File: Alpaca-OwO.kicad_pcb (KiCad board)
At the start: 4 copper layers, 100 x 45 mm, 43 parts, among them J1 SWD, J2 PS360 ST1, J3 PS360 ST2, J4 Stick, J5 USB_B, J6 Pwny Pr0t, J7 I2C Quick connect, Q1 CJL3415, SW1 Reset, SW2 I2C Pullup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

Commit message: Coarse placement
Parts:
- moved H2 118.6 mm to (115.0, 51.5)
- moved H4 115.6 mm to (206.0, 89.0)
- moved C14 88.3 mm to (161.8, 73.0), turned to 180 degrees
- moved C7 88.1 mm to (161.8, 71.5)
- moved H1 87.9 mm to (115.0, 89.5)
- moved C12 75.8 mm to (157.0, 78.5), turned to 90 degrees
- moved C10 75.6 mm to (153.5, 65.5), turned to -90 degrees
- moved C15 66.2 mm to (153.5, 78.8), turned to 90 degrees
- moved C13 63.5 mm to (148.5, 72.0)
- moved C9 61.6 mm to (159.0, 67.5), turned to 180 degrees
- moved C8 49.5 mm to (161.8, 74.5), turned to 180 degrees
- moved C16 43.0 mm to (169.0, 68.5), turned to -90 degrees
- moved C1 22.4 mm to (182.0, 63.5), turned to 90 degrees
- moved C6 21.2 mm to (148.5, 74.0)
- moved Q1 18.1 mm to (185.4, 72.4), turned to -90 degrees
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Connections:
- C6 pad 1: +1V1 -> GND
- C6 pad 2: GND -> +1V1
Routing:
- added copper zone on In2.Cu, net GND

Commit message: Routing checkpoint
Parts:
- Y1: footprint Crystal:Crystal_HC49-U_Vertical -> Crystal:Crystal_HC49-4H_Vertical
- moved SW1 57.5 mm to (178.6, 76.0), turned to 180 degrees
- moved R1 19.4 mm to (146.8, 75.5)
- moved C11 9.28 mm to (160.2, 74.8)
- moved C5 9.28 mm to (160.2, 76.2)
- moved SW3 9.24 mm to (178.6, 68.0), turned to 180 degrees
- moved C8 5.17 mm to (158.5, 78.5), turned to -90 degrees
- moved R3 4.03 mm to (165.5, 74.5)
- moved R4 4.02 mm to (165.5, 72.9)
- moved H1 2.06 mm to (117.0, 89.0)
- moved H2 2.06 mm to (117.0, 52.0)
- moved H3 2.00 mm to (205.0, 52.0)
- moved R2 1.95 mm to (146.8, 71.0), turned to 0 degrees
- moved C13 1.82 mm to (146.8, 72.5)
- moved Y1 1.80 mm to (139.8, 75.4)
- moved C6 1.75 mm to (146.8, 74.0)
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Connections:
- net Net-(R3-Pad1) renamed /UPIN_D+
- net Net-(R4-Pad1) renamed /UPIN_D-
- C4 pad 1: Net-(C4-Pad1) -> GND
- C4 pad 2: GND -> Net-(R2-Pad1)
- C8 pad 1: GND -> +3V3
- C8 pad 2: +3V3 -> GND
- R2 pad 1: Net-(C4-Pad1) -> Net-(R2-Pad1)
- Y1 pad 1: Net-(C4-Pad1) -> Net-(R2-Pad1)
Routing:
- net /~{RESET}: track 0.00 -> 62.4 mm, vias 0 -> 3
- net /I2C0_SDA: track 0.00 -> 61.7 mm, vias 0 -> 2
- net /I2C0_SCL: track 0.00 -> 57.9 mm, vias 0 -> 4
- net +3V3: track 0.00 -> 48.5 mm, vias 0 -> 8
- net /KEY_TP: track 0.00 -> 40.2 mm, vias 0 -> 1
- net /SPI0_DI: track 0.00 -> 37.9 mm, vias 0 -> 1
- net /USB_D+: track 0.00 -> 34.6 mm
- net /USB_D-: track 0.00 -> 34.0 mm
- net /SPI0_CLK: track 0.00 -> 34.0 mm, vias 0 -> 1
- net /SPI0_CS: track 0.00 -> 33.1 mm, vias 0 -> 1
- net /UART1_TX: track 0.00 -> 31.1 mm, vias 0 -> 1
- net /SPI0_DO: track 0.00 -> 29.5 mm, vias 0 -> 1
- net /KEY_L3: track 0.00 -> 29.0 mm, vias 0 -> 1
- net +1V1: track 0.00 -> 28.2 mm, vias 0 -> 3
- net /UART1_RX: track 0.00 -> 27.0 mm, vias 0 -> 1
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- added copper zone on In1.Cu, net +3V3
- added copper zone on In2.Cu, net +3V3
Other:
- rule pad_to_mask_clearance: 0 -> 0.05
- board text added: "OwO"

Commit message: First PnR attempt done.
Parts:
- moved J4 28.8 mm to (128.8, 86.1), turned to 90 degrees
- moved SW1 1.30 mm to (178.6, 77.3)
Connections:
- J5 pad 5: unconnected-(J5-Pad5) -> (no net)
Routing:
- net /DBTN_D: track 0.00 -> 45.1 mm, vias 0 -> 1
- net /DBTN_U: track 0.00 -> 42.1 mm, vias 0 -> 1
- net /DBTN_L: track 0.00 -> 39.2 mm, vias 0 -> 1
- net /DBTN_R: track 0.00 -> 36.3 mm, vias 0 -> 1
- net /KEY_L2: track 0.00 -> 31.6 mm, vias 0 -> 2
- net /STK_LX: track 0.00 -> 31.3 mm, vias 0 -> 2
- net /STK_LY: track 0.00 -> 29.7 mm, vias 0 -> 2
- net /KEY_R2: track 0.00 -> 28.7 mm, vias 0 -> 2
- net /STK_RX: track 0.00 -> 27.9 mm, vias 0 -> 2
- net /KEY_PS: track 0.00 -> 27.6 mm, vias 0 -> 1
- net /STK_RY: track 0.00 -> 26.1 mm, vias 0 -> 2
- net /KEY_CIR: track 0.00 -> 25.1 mm, vias 0 -> 2
- net /KEY_SHR: track 0.00 -> 23.2 mm, vias 0 -> 1
- net /SWDIO: track 0.00 -> 22.8 mm, vias 0 -> 1
- net /KEY_XRO: track 0.00 -> 21.3 mm, vias 0 -> 2
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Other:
- board text added: "3V3"
- board text added: "Alpaca-OwO v1.0 Hacker friendly arcade controller I/O platform. Proudly based on RP2040"
- board text added: "BootSel"
- board text added: "C"
- board text added: "CIR"
- board text added: "CS DI"
- board text added: "D"
- board text added: "DO CLK"
- board text added: "EXT"
- board text added: "GND"
- board text added: "I/O"
- board text added: "I2C Pullup"
- board text added: "I2C QC"
- board text added: "I2C0"
- board text added: "JLCJLCJLCJLC"
- board text added: "L"
- board text added: "L1"
- board text added: "L2"
- board text added: "L3"
- board text added: "LX"
- board text added: "LY"
- board text added: "OPT"
- board text added: "PS"
- board text added: "R"
- board text added: "R1"
- board text added: "R2"
- board text added: "R3"
- board text added: "R3 L3"
- board text added: "RX"
- board text added: "RX TX"
- board text added: "RY"
- board text added: "Reset"
- board text added: "SCL SDA"
- board text added: "SHR"
- board text added: "SPI0"
- board text added: "SQR"
- board text added: "SWD"
- board text added: "Stick"
- board text added: "TP GND"
- board text added: "TRI"
- board text added: "U"
- board text added: "UART1"
- board text added: "XRO"
- board text added: "~{R}"

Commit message: More ground vias.
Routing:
- net +1V1: track 28.0 -> 27.4 mm
- net +3V3: track 52.3 -> 51.8 mm
- net GND: vias 6 -> 17
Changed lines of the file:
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@@
   (segment (start 151.0625 71.5) (end 152 71.5) (width 0.25) (layer "F.Cu") (net 2))
   (segment (start 185.5 87.25) (end 185.5 86) (width 0.25) (layer "F.Cu") (net 2))
+  (via (at 188 62.2) (size 0.5) (drill 0.3) (layers "F.Cu" "B.Cu") (free) (net 2))
+  (via (at 188 64.8) (size 0.5) (drill 0.3) (layers "F.Cu" "B.Cu") (free) (net 2))
+  (via (at 198.4 63.5) (size 0.5) (drill 0.3) (layers "F.Cu" "B.Cu") (free) (net 2))
   (via (at 184.5 70) (size 0.4) (drill 0.2) (layers "F.Cu" "B.Cu") (free) (net 2))
+  (via (at 167.3 66.8) (size 0.4) (drill 0.2) (layers "F.Cu" "B.Cu") (free) (net 2))
+  (via (at 158 64.8) (size 0.5) (drill 0.3) (layers "F.Cu" "B.Cu") (free) (net 2))
+  (via (at 160 79.3) (size 0.5) (drill 0.3) (layers "F.Cu" "B.Cu") (free) (net 2))
   (via (at 152 71.5) (size 0.5) (drill 0.3) (layers "F.Cu" "B.Cu") (net 2))
+  (via (at 144.3 72.5) (size 0.5) (drill 0.3) (layers "F.Cu" "B.Cu") (free) (net 2))
+  (via (at 163.2 72) (size 0.5) (drill 0.3) (layers "F.Cu" "B.Cu") (free) (net 2))
+  (via (at 144.1 74) (size 0.5) (drill 0.3) (layers "F.Cu" "B.Cu") (free) (net 2))
   (via (at 185.5 86) (size 0.5) (drill 0.3) (layers "F.Cu" "B.Cu") (net 2))
   (via (at 163 63) (size 0.4) (drill 0.2) (layers "F.Cu" "B.Cu") (free) (net 2))
   (via (at 136 68) (size 0.5) (drill 0.3) (layers "F.Cu" "B.Cu") (net 2))
+  (via (at 153.5 63.6) (size 0.5) (drill 0.3) (layers "F.Cu" "B.Cu") (free) (net 2))
+  (via (at 152.2 79.3) (size 0.5) (drill 0.3) (layers "F.Cu" "B.Cu") (free) (net 2))
   (via (at 136 78) (size 0.5) (drill 0.3) (layers "F.Cu" "B.Cu") (net 2))
   (segment (start 185.575 82.425) (end 186 82) (width 0.25) (layer "F.Cu") (net 3))
@@
   (segment (start 158.45 74.7) (end 158.75 75) (width 0.25) (layer "F.Cu") (net 3))
   (segment (start 168.75 68.3) (end 168.75 69.25) (width 0.25) (layer "F.Cu") (net 3))
-  (segment (start 148.3 72.5) (end 148.3 73) (width 0.25) (layer "F.Cu") (net 3))
   (segment (start 185 82.425) (end 185.575 82.425) (width 0.25) (layer "F.Cu") (net 3))
   (segment (start 157.1 69.0625) (end 157.1 68.4) (width 0.25) (layer "F.Cu") (net 3))
@@
   (via (at 186 82) (size 0.5) (drill 0.3) (layers "F.Cu" "B.Cu") (net 3))
   (via (at 159.375 77.375) (size 0.5) (drill 0.3) (layers "F.Cu" "B.Cu") (net 3))
-  (via (at 148.3 73) (size 0.5) (drill 0.3) (layers "F.Cu" "B.Cu") (net 3))
+  (via (at 148.5 72.5) (size 0.5) (drill 0.3) (layers "F.Cu" "B.Cu") (net 3))
   (via (at 145.1 75.5) (size 0.5) (drill 0.3) (layers "F.Cu" "B.Cu") (net 3))
   (via (at 153.5 67.2) (size 0.5) (drill 0.3) (layers "F.Cu" "B.Cu") (net 3))
@@
   (segment (start 139.75 75.38) (end 136 75.38) (width 0.2) (layer "F.Cu") (net 5))
   (segment (start 139.75 73.75) (end 142.5 71) (width 0.2) (layer "F.Cu") (net 5))
-  (segment (start 148.55 73.55) (end 148.9 73.9) (width 0.25) (layer "F.Cu") (net 6))
   (segment (start 160.75 70.5) (end 161 70.5) (width 0.25) (layer "F.Cu") (net 6))
-  (segment (start 149 73.1) (end 148.55 73.55) (width 0.25) (layer "F.Cu") (net 6))
   (segment (start 159.025 74.3) (end 159.475 74.75) (width 0.25) (layer "F.Cu") (net 6))
   (segment (start 159.425 72.3) (end 160.475 71.25) (width 0.25) (layer "F.Cu") (net 6))
   (segment (start 160.475 70.775) (end 160.75 70.5) (width 0.25) (layer "F.Cu") (net 6))
   (segment (start 148.1 74) (end 147.525 74) (width 0.25) (layer "F.Cu") (net 6))
+  (segment (start 148.1 74) (end 149 73.1) (width 0.25) (layer "F.Cu") (net 6))
   (segment (start 159.475 74.975) (end 160 75.5) (width 0.25) (layer "F.Cu") (net 6))
   (segment (start 151.0625 73.1) (end 149 73.1) (width 0.25) (layer "F.Cu") (net 6))
   (segment (start 157.9375 74.3) (end 159.025 74.3) (width 0.25) (layer "F.Cu") (net 6))
-  (segment (start 148.9 73.9) (end 148.9 74.4) (width 0.25) (layer "F.Cu") (net 6))
-  (segment (start 148.55 73.55) (end 148.1 74) (width 0.25) (layer "F.Cu") (net 6))
   (segment (start 157.9375 72.3) (end 159.425 72.3) (width 0.25) (layer "F.Cu") (net 6))
   (segment (start 160.475 71.25) (end 160.475 70.775) (width 0.25) (layer "F.Cu") (net 6))
   (via (at 161 70.5) (size 0.5) (drill 0.3) (layers "F.Cu" "B.Cu") (net 6))
   (via (at 160 75.5) (size 0.4) (drill 0.2) (layers "F.Cu" "B.Cu") (net 6))
-  (via (at 148.9 74.4) (size 0.5) (drill 0.3) (layers "F.Cu" "B.Cu") (net 6))
-  (segment (start 160 74.4) (end 160 75.5) (width 0.25) (layer "In1.Cu") (net 6))
+  (via (at 148.6 73.5) (size 0.5) (drill 0.3) (layers "F.Cu" "B.Cu") (net 6))
+  (segment (start 149.000011 73.099989) (end 148.6 73.5) (width 0.25) (layer "In1.Cu") (net 6))
+  (segment (start 160 73.1) (end 159.7 73.1) (width 0.25) (layer "In1.Cu") (net 6))
+  (segment (start 159.699989 73.099989) (end 149.000011 73.099989) (width 0.25) (layer "In1.Cu") (net 6))
+  (segment (start 160 71.5) (end 160 75.5) (width 0.25) (layer "In1.Cu") (net 6))
   (segment (start 161 70.5) (end 160 71.5) (width 0.25) (layer "In1.Cu") (net 6))
-  (segment (start 148.9 74.4) (end 160 74.4) (width 0.25) (layer "In1.Cu") (net 6))
-  (segment (start 160 71.5) (end 160 74.4) (width 0.25) (layer "In1.Cu") (net 6))
+  (segment (start 159.7 73.1) (end 159.699989 73.099989) (width 0.25) (layer "In1.Cu") (net 6))
   (segment (start 191.9 72.41) (end 195.4225 72.41) (width 1) (layer "F.Cu") (net 7))
   (segment (start 187.5075 72.41) (end 186.37 73.5475) (width 1) (layer "F.Cu") (net 8))
@@
   (zone (net 2) (net_name "GND") (layers "F.Cu" "In2.Cu" "B.Cu") (name "Ground") (hatch edge 0.508)
     (priority 1)
-    (connect_pads (clearance 0.508))
+    (connect_pads (clearance 0.254))
     (min_thickness 0.254) (filled_areas_thickness no)
     (fill yes (thermal_gap 0.508) (thermal_bridge_width 0.508))
@@
   )
   (zone (net 3) (net_name "+3V3") (layer "In1.Cu") (name "3V3") (hatch edge 0.508)
-    (connect_pads (clearance 0.508))
+    (connect_pads (clearance 0.254))
     (min_thickness 0.254) (filled_areas_thickness no)
     (fill yes (thermal_gap 0.508) (thermal_bridge_width 0.508))

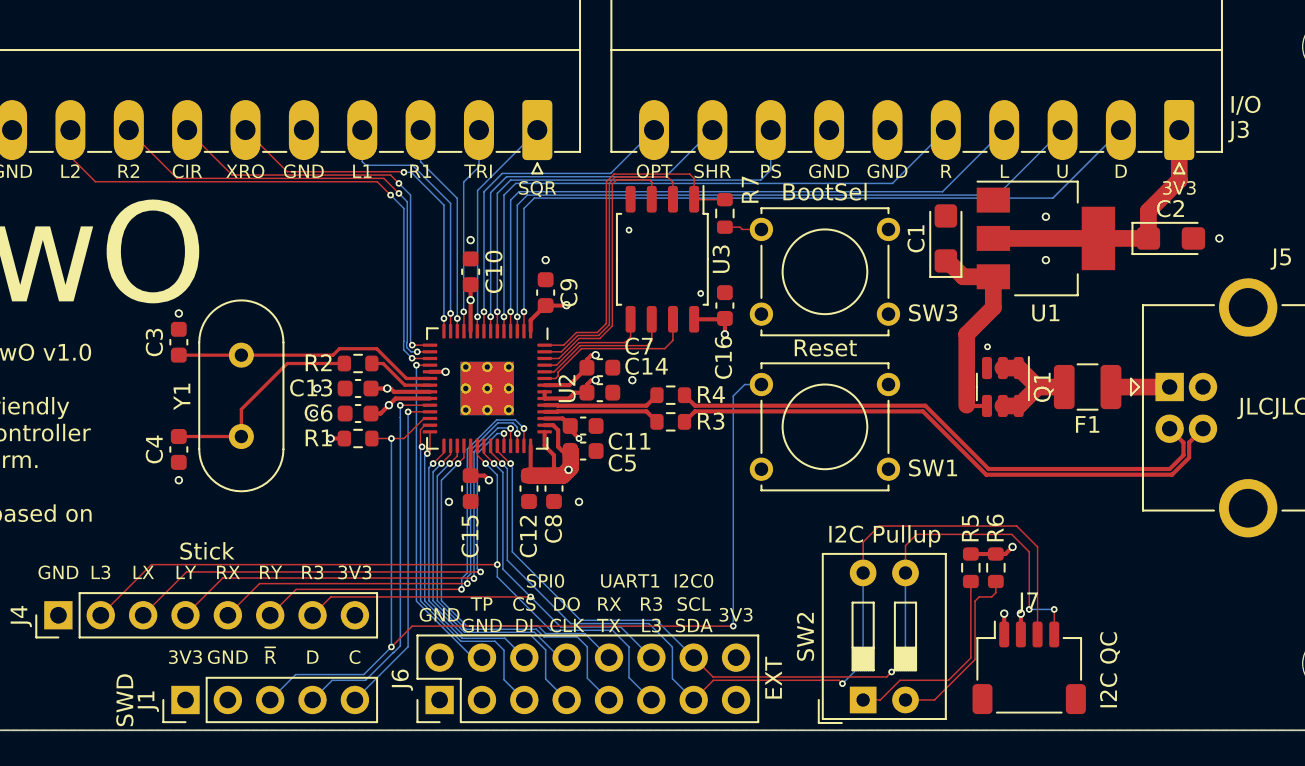
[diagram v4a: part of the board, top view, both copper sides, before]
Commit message: Fix various issues.
- USB DM/DP are reversed.
- Minimum via OD for JLC should be 0.45mm (technically 0.4mm is also accepted but with a big cost penalty).
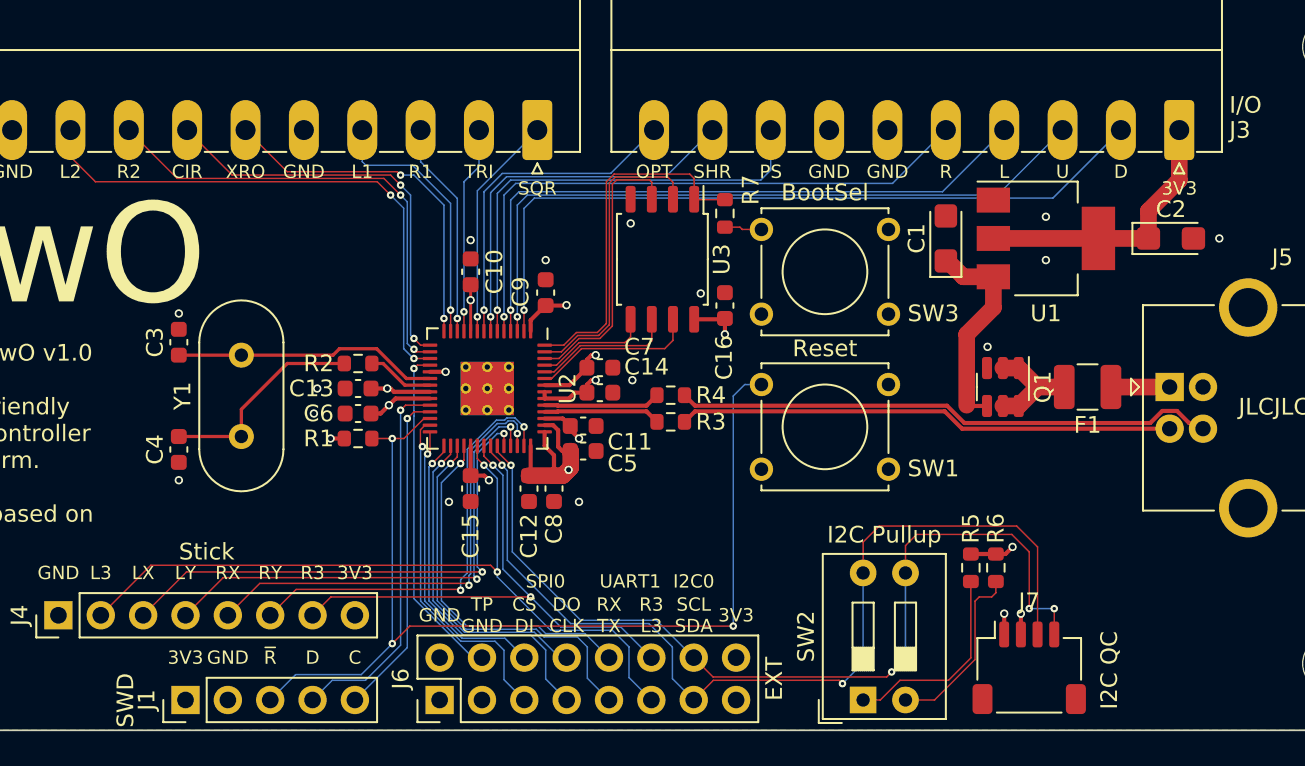
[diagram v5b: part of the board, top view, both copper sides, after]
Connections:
- R3 pad 1: /UPIN_D+ -> /UPIN_D-
- R3 pad 2: /USB_D+ -> /USB_D-
- R4 pad 1: /UPIN_D- -> /UPIN_D+
- R4 pad 2: /USB_D- -> /USB_D+
- U2 pad 46: /UPIN_D+ -> /UPIN_D-
- U2 pad 47: /UPIN_D- -> /UPIN_D+
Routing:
- net /USB_D-: track 34.0 -> 29.8 mm
- net /USB_D+: track 34.6 -> 32.0 mm

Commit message: V1.01 rework.
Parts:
- SW1, SW3: footprint Button_Switch_THT:SW_Tactile_Straight_KSA0Axx1LFTR -> Button_Switch_THT:SW_PUSH_6mm
- moved C15 31.5 mm to (148.2, 109.5)
- moved C12 31.5 mm to (151.8, 109.5)
- moved C16 31.2 mm to (163.1, 98.2)
- moved U3 31.1 mm to (159.4, 95.3)
- moved R7 31.1 mm to (163.1, 92.6)
- moved J5 30.9 mm to (188.0, 102.5)
- moved C1 30.5 mm to (191.4, 92.5), turned to 180 degrees
- moved J4 30.5 mm to (123.5, 116.2)
- moved C10 30.5 mm to (148.2, 95.5)
- moved C13 30.5 mm to (141.4, 102.5)
- moved C14 30.5 mm to (155.9, 102.8)
- moved C6 30.5 mm to (141.4, 104.0)
- moved C7 30.5 mm to (155.9, 101.3)
- moved C9 30.5 mm to (152.7, 96.8)
- moved H1 30.5 mm to (111.7, 119.0)
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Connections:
- SW1 pad 1: GND -> /~{RESET}
- SW1 pad 2: /~{RESET} -> GND
- SW3 pad 1: GND -> Net-(R7-Pad1)
- SW3 pad 2: Net-(R7-Pad1) -> GND
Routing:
- net +1V1: track 27.4 -> 9.90 mm
- net /~{RESET}: track 61.3 -> 54.4 mm, vias 3 -> 2
- net /I2C0_SCL: track 54.9 -> 49.8 mm, vias 4 -> 2
- net Net-(C1-Pad1): track 12.7 -> 17.2 mm
- net /USB_D-: track 29.8 -> 25.7 mm
- net +3V3: track 51.8 -> 48.2 mm, vias 10 -> 14
- net /USB_D+: track 32.0 -> 28.5 mm
- net /KEY_PS: track 27.6 -> 24.1 mm, vias 1 -> 0
- net Net-(R7-Pad1): track 2.25 -> 5.60 mm
- net /STK_RY: track 26.2 -> 23.1 mm, vias 2 -> 1
- net /STK_RX: track 28.3 -> 25.3 mm, vias 2 -> 1
- net /UART1_TX: track 23.7 -> 20.7 mm, vias 1 -> 0
- net /UART1_RX: track 21.3 -> 18.5 mm, vias 1 -> 0
- net /STK_LY: track 30.1 -> 27.5 mm, vias 2 -> 1
- net /KEY_SHR: track 23.2 -> 20.9 mm, vias 1 -> 0
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- added copper zone on In2.Cu, net +1V1
- added copper zone on In1.Cu, net GND
- removed copper zone on In1.Cu, net +3V3
- removed copper zone on In2.Cu, net GND
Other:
- board size 100 x 45 mm -> 96 x 45 mm
- board text added: "Alpaca-OwO v1.01 Hacker friendly arcade controller I/O platform. Proudly based on RP2040"
- board text removed: "Alpaca-OwO v1.0 Hacker friendly arcade controller I/O platform. Proudly based on RP2040"

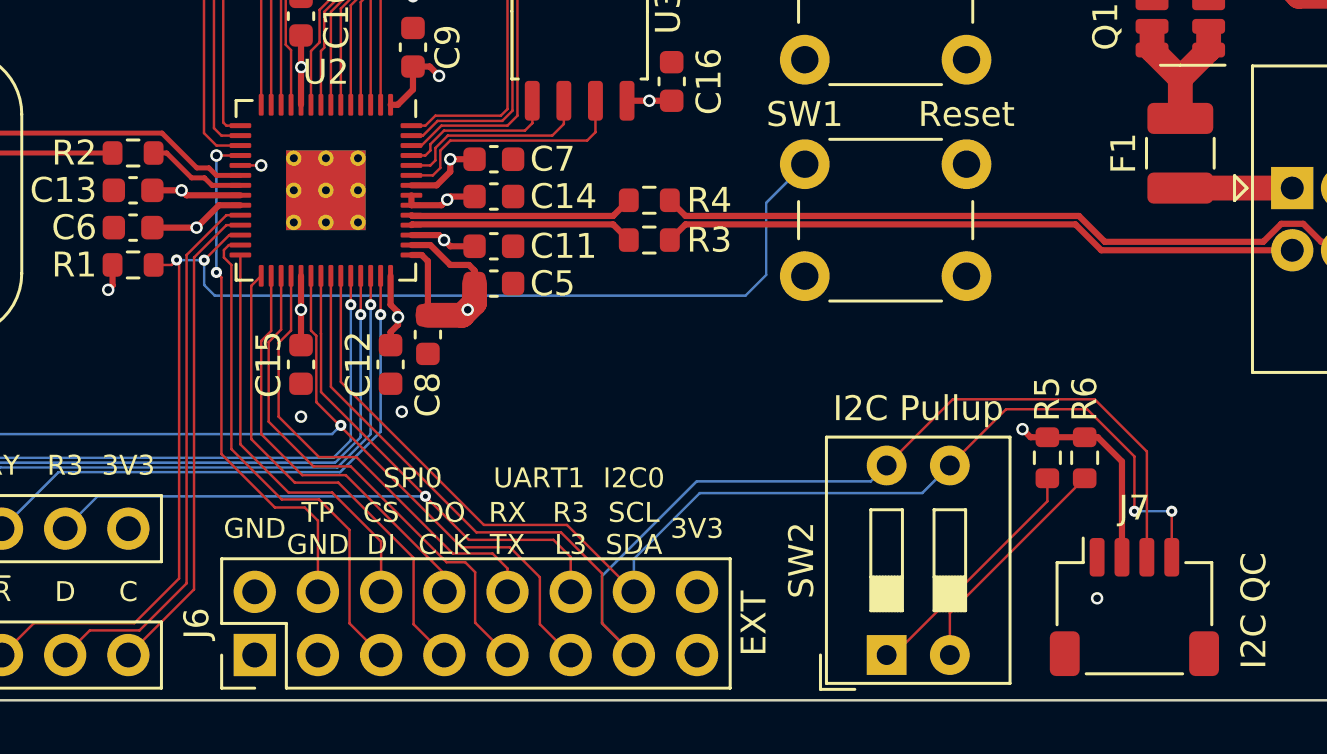
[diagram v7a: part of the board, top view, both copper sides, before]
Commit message: Flip I2C traces up and some general cleanups
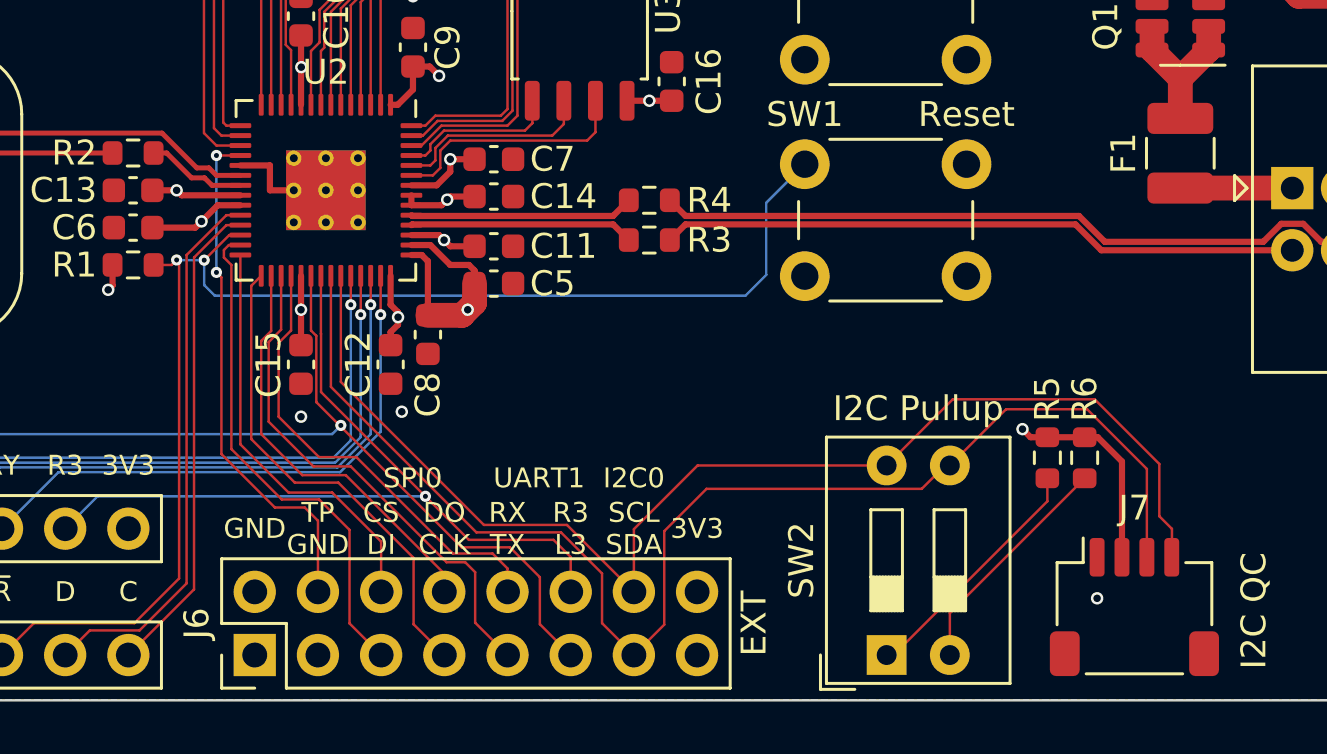
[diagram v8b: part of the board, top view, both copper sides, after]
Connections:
- SW2 pad 3: /I2C0_SCL -> /I2C0_SDA
- SW2 pad 4: /I2C0_SDA -> /I2C0_SCL
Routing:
- net GND: track 0.84 -> 4.56 mm, vias 11 -> 10
- net /I2C0_SDA: track 56.0 -> 53.5 mm
- net /I2C0_SCL: track 49.8 -> 50.4 mm, vias 2 -> 0
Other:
- board text added: "The ADC traces are currently routed on the back of the board on top of power plane. This is less than ideal but should be OK if they are only used for low freq low res ADC sampling (e.g. as analog sticks). Resolving this would require shifting a large amount of components or even redo the whole board so might not be worth it for now."
